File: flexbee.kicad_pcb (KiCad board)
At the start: 4 copper layers, 30.7 x 17.6 mm, 68 parts, among them J1 Conn_01x12_Male, J2 Conn_01x12_Male, U1 SSD210, U2 ea3056, U3 spinor, Y1 Crystal_GND24

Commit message: Add files via upload
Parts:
- added C24: C, Capacitor_SMD:C_0402_1005Metric, B.Cu at (142.6, 96.1)
- added C25: C, Capacitor_SMD:C_0402_1005Metric, B.Cu at (143.6, 96.1)
- added C26: C, Capacitor_SMD:C_0402_1005Metric, B.Cu at (140.1, 95.4)
- added C27: C, Capacitor_SMD:C_0402_1005Metric, B.Cu at (146.3, 90.1)
- added C28: C, Capacitor_SMD:C_0402_1005Metric, B.Cu at (140.4, 92.4)
- added C29: C, Capacitor_SMD:C_0402_1005Metric, B.Cu at (142.4, 89.6)
- added C30: C, Capacitor_SMD:C_0402_1005Metric, B.Cu at (147.1, 93.3)
- added C31: C, Capacitor_SMD:C_0603_1608Metric, B.Cu at (158.4, 95.3)
- added C32: C, Capacitor_SMD:C_0603_1608Metric, B.Cu at (151.7, 94.6)
- added C33: C, Capacitor_SMD:C_0603_1608Metric, B.Cu at (158.4, 89.5)
- added R18: R, Resistor_SMD:R_0402_1005Metric, B.Cu at (159.2, 93.5)
- added R19: R, Resistor_SMD:R_0402_1005Metric, B.Cu at (159.2, 91.2)
- C10, C22, C23, R16: moved to B.Cu
- C13, R11, R9: moved to F.Cu
- moved C10 28.0 mm to (130.4, 88.7), turned to -90 degrees
- moved U3 22.6 mm to (132.4, 92.2), turned to 90 degrees
- moved TP1 17.3 mm to (147.3, 98.5)
- moved TP14 15.5 mm to (139.7, 86.6)
- moved TP2 15.0 mm to (149.9, 98.5)
- moved TP6 15.0 mm to (152.4, 98.5)
- moved C22 14.5 mm to (144.6, 96.1), turned to 90 degrees
- moved TP4 14.1 mm to (154.9, 86.6)
- moved TP8 14.1 mm to (157.5, 86.6)
- moved R16 13.8 mm to (140.3, 97.6)
- moved R17 13.1 mm to (152.8, 88.1)
- moved TP5 12.5 mm to (144.8, 98.5)
- moved C16 11.5 mm to (140.2, 96.5)
- moved C14 11.3 mm to (141.6, 96.1), turned to 90 degrees
- moved C13 11.3 mm to (141.0, 87.5)
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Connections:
- J1 pad 1: VCC -> +3V3
- J1 pad 10: /lineout -> /usb_dp
- J1 pad 11: +3V3 -> VCC
- J1 pad 3: /sar_gpio0 -> /lineout
- J1 pad 4: /sar_gpio1 -> /sar_gpio0
- J1 pad 5: /sar_gpio2 -> /sar_gpio1
- J1 pad 6: /uart_rx -> /sar_gpio2
- J1 pad 7: /uart_tx -> /uart_rx
- J1 pad 8: /usb_dm -> /uart_tx
- J1 pad 9: /usb_dp -> /usb_dm
- J2 pad 1: /ttl8 -> /ttl21
- J2 pad 10: /ttl19 -> /ttl13
- J2 pad 11: /ttl20 -> /ttl8
- J2 pad 12: /ttl21 -> /ttl11
- J2 pad 2: /ttl11 -> /ttl20
- J2 pad 3: /ttl12 -> /ttl19
- J2 pad 4: /ttl13 -> /ttl18
- J2 pad 5: /ttl14 -> /ttl17
- J2 pad 6: /ttl15 -> /ttl16
- J2 pad 7: /ttl16 -> /ttl15
- J2 pad 8: /ttl17 -> /ttl14
- J2 pad 9: /ttl18 -> /ttl12
- TP1 pad 1: Net-(TP1-Pad1) -> /i2c0_sda
- TP5 pad 1: Net-(TP5-Pad1) -> /i2c0_scl
- U1 pad 29: Net-(TP1-Pad1) -> /i2c0_scl
- U1 pad 30: Net-(TP5-Pad1) -> /i2c0_sda
- U2 pad 15: unconnected-(U2-Pad15) -> /i2c0_sda
- U2 pad 16: unconnected-(U2-Pad16) -> /i2c0_scl
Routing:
- net /flash_mosi: track 53.7 -> 7.93 mm, vias 2 -> 0
- net /flash_hld: track 53.7 -> 10.7 mm, vias 2 -> 0
- net +3V3: track 67.5 -> 25.7 mm, vias 6 -> 8
- net /flash_clk: track 51.7 -> 10.3 mm, vias 2 -> 0
- net /i2c0_sda: track 0.00 -> 37.6 mm, vias 0 -> 2
- net /i2c0_scl: track 0.00 -> 36.9 mm, vias 0 -> 2
- net GND: track 3.70 -> 36.6 mm
- net /flash_wpz: track 40.2 -> 10.1 mm, vias 2 -> 0
- net +1V0: track 48.0 -> 18.6 mm, vias 3 -> 4
- net /flash_miso: track 35.4 -> 11.8 mm
- net /flash_cs: track 33.7 -> 14.5 mm
- net /lineout: track 26.9 -> 8.14 mm, vias 1 -> 0
- net +1V8: track 29.2 -> 13.2 mm, vias 2 -> 3
- net /usb_dp: track 15.4 -> 0.00 mm
- net Net-(TP14-Pad1): track 34.7 -> 21.5 mm
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- added copper zone on In2.Cu, net +1V0
- added copper zone on In2.Cu, net +1V8
- added copper zone on In2.Cu, net +3V3
- added copper zone on F.Cu, net Net-(L1-Pad2)
- added copper zone on F.Cu, net Net-(L2-Pad1)
- added copper zone on F.Cu, net Net-(L3-Pad1)
- added copper zone on In2.Cu, net VBUS
- added copper zone on F.Cu, net VCC
- added copper zone on In2.Cu, net VCC
- removed copper zone on B.Cu, net GND
- removed copper zone on In2.Cu, net GND
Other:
- board size 30.7 x 17.6 mm -> 30.8 x 17.6 mm

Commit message: Finished laying you the board
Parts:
- moved R11 3.21 mm to (136.6, 89.1), turned to -90 degrees
- moved C11 1.63 mm to (138.6, 89.1), turned to -90 degrees
- moved R17 0.52 mm to (153.3, 88.1)
- moved R9 0.25 mm to (137.6, 89.1), turned to 90 degrees
- moved C13 0.18 mm to (141.0, 87.7)
- moved R4 0.10 mm to (150.9, 90.6)
- moved R8 0.08 mm to (150.3, 93.9)
- moved R10 0.07 mm to (143.9, 88.1)
- moved C32 0.07 mm to (151.8, 94.6)
- moved C17 0.06 mm to (137.9, 92.4)
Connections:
- net /usb_dm renamed /usb-
- net /usb_dp renamed /usb+
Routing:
- net +3V3: track 25.7 -> 39.0 mm, vias 8 -> 7
- net /usb+: track 0.00 -> 10.7 mm
- net /usb-: track 1.73 -> 10.7 mm
- net GND: track 36.6 -> 43.7 mm, vias 24 -> 23
- net Net-(C13-Pad1): track 2.77 -> 6.76 mm
- net /ttl15: track 15.8 -> 13.8 mm
- net Net-(C2-Pad2): track 4.42 -> 5.95 mm, vias 2 -> 1
- net /sar_gpio0: track 7.49 -> 9.00 mm
- net /lineout: track 8.14 -> 9.28 mm
- net Net-(C11-Pad1): track 4.14 -> 3.05 mm
- net Net-(C11-Pad2): track 4.20 -> 3.17 mm
- net +1V8: track 13.2 -> 12.2 mm
- net Net-(C12-Pad2): track 5.58 -> 6.38 mm
- net /sar_gpio1: track 5.71 -> 6.32 mm
- net Net-(TP9-Pad1): track 11.4 -> 12.0 mm, vias 1 -> 0
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
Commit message: Layout Fixes
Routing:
- net Net-(TP9-Pad1): vias 0 -> 1
- net Net-(TP6-Pad1): vias 0 -> 1
- net Net-(TP3-Pad1): vias 0 -> 1
- net Net-(TP2-Pad1): vias 0 -> 1
- net Net-(TP16-Pad1): vias 0 -> 1
- net Net-(TP15-Pad1): vias 0 -> 1
- net Net-(TP11-Pad1): vias 0 -> 1
- net Net-(TP10-Pad1): vias 0 -> 1

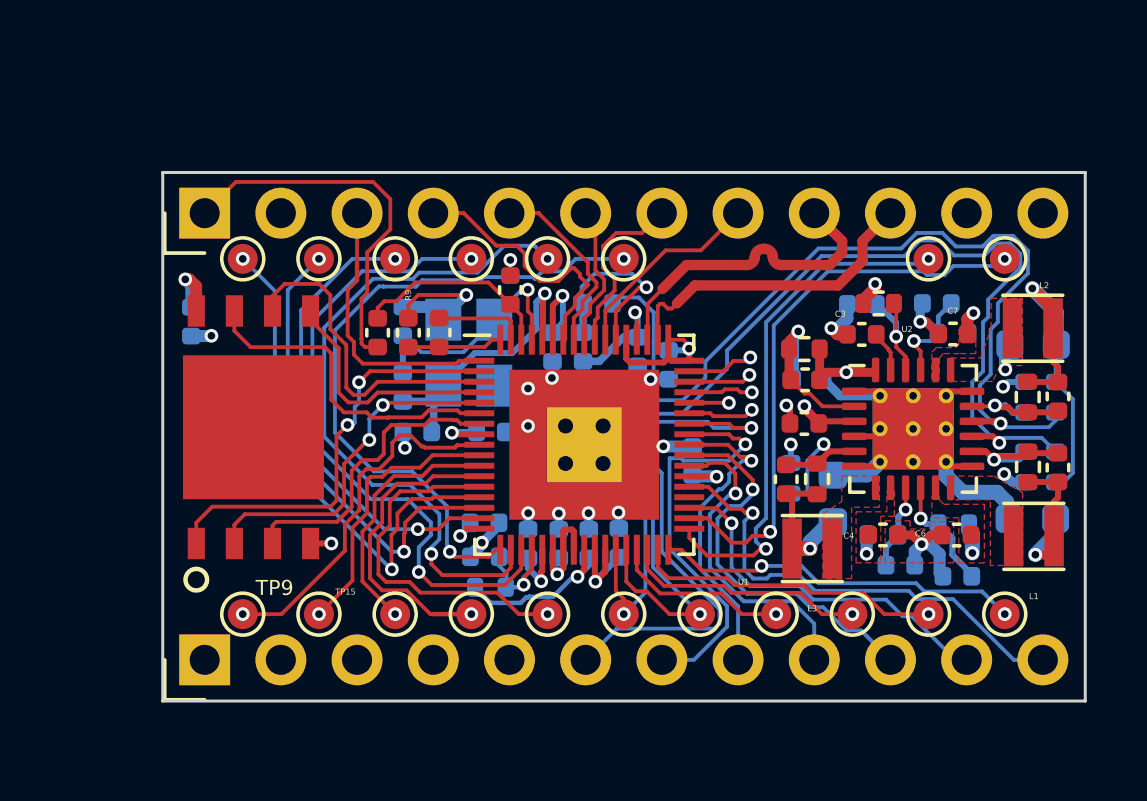
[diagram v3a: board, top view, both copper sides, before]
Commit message: Update boot resistors added
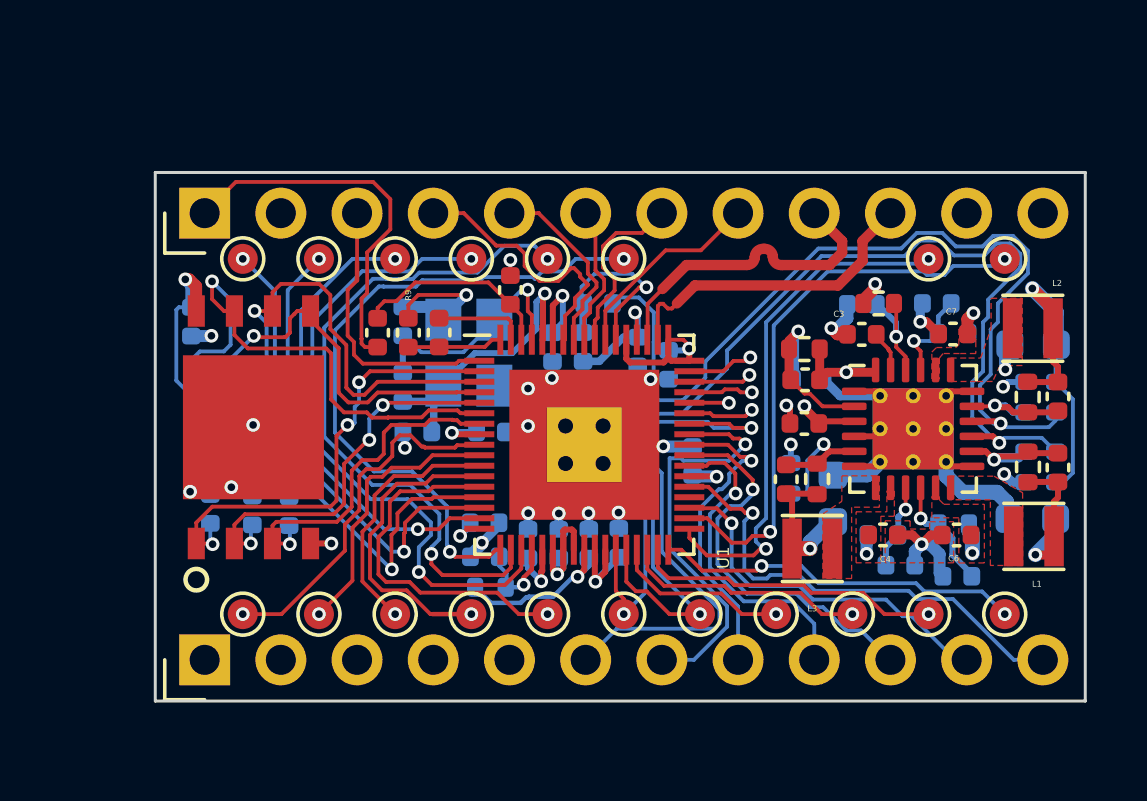
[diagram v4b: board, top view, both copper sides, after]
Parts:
- added R20: R, Capacitor_SMD:C_0402_1005Metric, B.Cu at (132.6, 90.8)
- added R21: R, Capacitor_SMD:C_0402_1005Metric, B.Cu at (132.4, 95.0)
- added R22: R, Capacitor_SMD:C_0402_1005Metric, B.Cu at (130.4, 90.8)
- added R23: R, Capacitor_SMD:C_0402_1005Metric, B.Cu at (133.6, 95.0)
- added R24: R, Capacitor_SMD:C_0402_1005Metric, B.Cu at (131.5, 90.8)
- added R25: R, Capacitor_SMD:C_0402_1005Metric, B.Cu at (131.0, 95.0)
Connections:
- U3 pad 9: (no net) -> GND
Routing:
- net +3V3: track 39.0 -> 51.1 mm
- net /flash_hld: track 11.1 -> 16.8 mm, vias 0 -> 1
- net /flash_mosi: track 8.12 -> 12.1 mm, vias 0 -> 1
- net /flash_clk: track 10.8 -> 13.6 mm, vias 0 -> 1
- net GND: track 43.7 -> 45.6 mm, vias 23 -> 26
- net /flash_cs: track 14.2 -> 15.5 mm, vias 2 -> 3
- net /flash_wpz: track 10.1 -> 11.4 mm, vias 0 -> 1
- net /flash_miso: track 11.7 -> 12.9 mm, vias 2 -> 3
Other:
- board size 30.8 x 17.6 mm -> 31 x 17.6 mm

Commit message: Clean-up
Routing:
- net /sar_gpio0: track 9.00 -> 7.93 mm

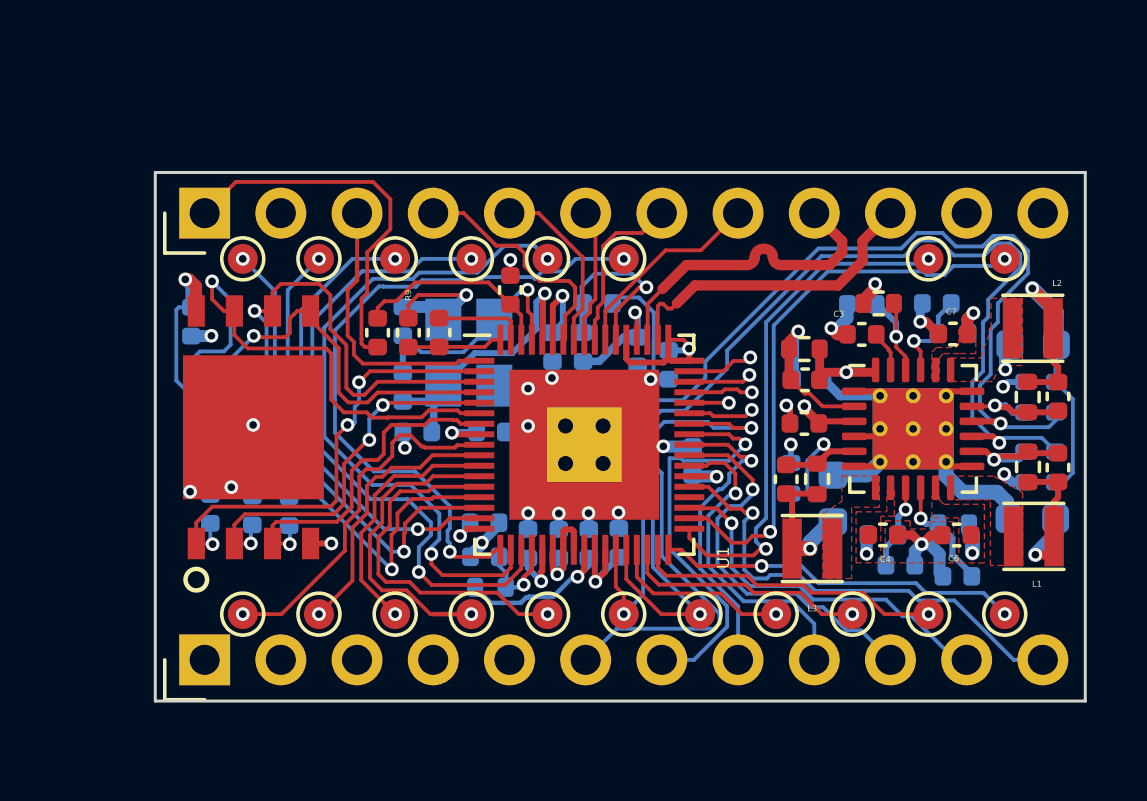
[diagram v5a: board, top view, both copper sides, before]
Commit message: Silkscreen adjustment
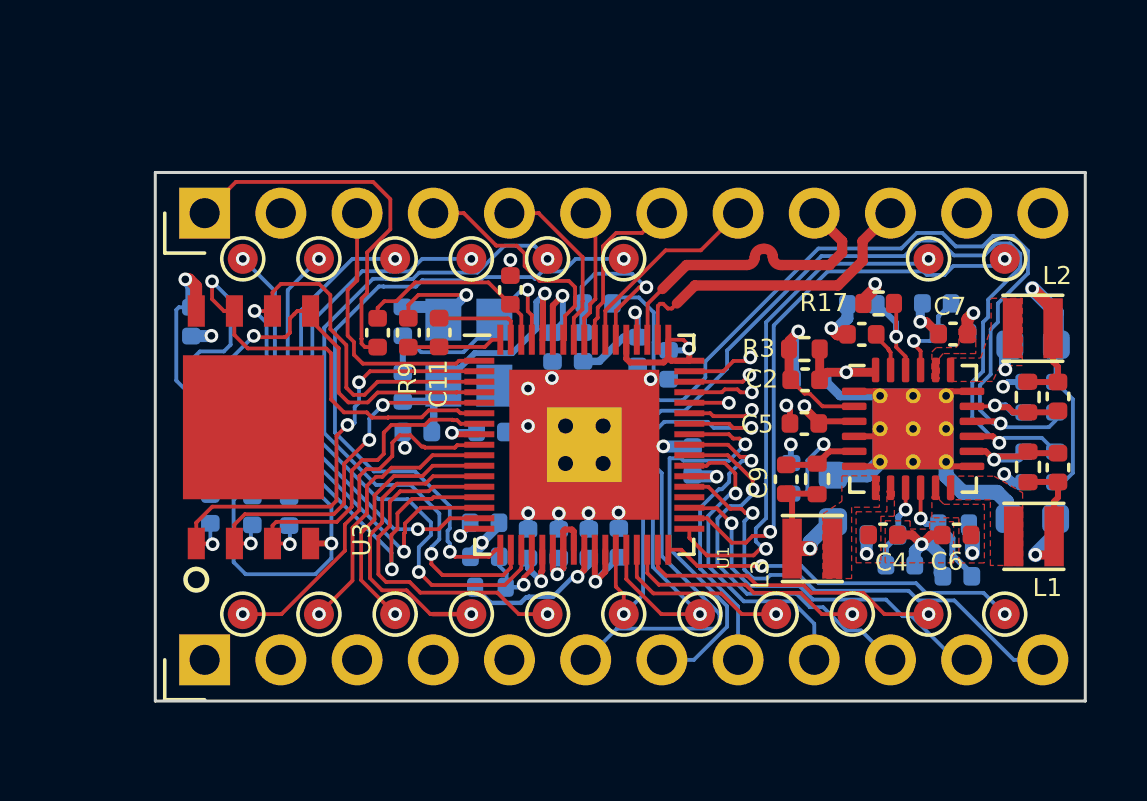
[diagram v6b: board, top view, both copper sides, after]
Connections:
- U3 pad 9: GND -> (no net)
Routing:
- net GND: track 45.6 -> 56.6 mm, vias 26 -> 23

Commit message: A few little touches
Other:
- board text added: "predita rev0"

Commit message: Sync with my local machine
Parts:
- R10, R11, R12, R20, R21, R22, R23, R24, R25, R9: footprint Capacitor_SMD:C_0402_1005Metric -> Resistor_SMD:R_0402_1005Metric
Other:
- board text added: "(at)linux-chenxing"
- board text added: "bzz!"
